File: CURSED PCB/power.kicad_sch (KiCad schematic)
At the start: 22 parts, among them J3 2 Wire Block for laser, J5 G125-MH104M4-04AD000P, U1 MIC94090YC6, U2 INA180, U4 SPX3819M5-L-3-3, U5 MCP1754S-3302xCB

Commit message: fix with ash
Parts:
- removed U5: MCP1754S-3302xCB, Package_TO_SOT_SMD:SOT-23, symbol Regulator_Linear:MCP1754S-3302xCB
- added U5: SPX3819M5-L-3-3, Package_TO_SOT_SMD:SOT-23-5, symbol Regulator_Linear:SPX3819M5-L-3-3
- C10: value 1uF -> 10nF
- C13: value 10uF -> 1uF
- F1: value 600mA -> 1A
- R6: value 55m -> 33m
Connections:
- net +3.3VA: now also U5.5 (OUT); no longer C10.1
- net +5V: now also U5.1 (IN), U5.3 (EN)
- net GND: now also U5.2 (GND)
- new net: C10.1, U5.4 (BP)
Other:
- note added: "100 V/V Gain or 40dB"
- note added: "R_shunt = (VOUT / GAIN)/ Current VOUT = 3.3 Gain = 100 Current = 1A R_shunt = 33 mohm"
- note removed: "100 Gain"
- moved on the sheet: C10
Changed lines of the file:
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@@
 	(generator_version "9.0")
 	(paper "A4")
-	(text "100 Gain\n"
+	(text "R_shunt = (VOUT / GAIN)/ Current\n\nVOUT = 3.3\nGain = 100\nCurrent = 1A\nR_shunt = 33 mohm"
 		(exclude_from_sim no)
-		(at 103.886 78.232 0)
+		(at 65.786 43.688 0)
+		(effects
+			(font
+				(size 1.27 1.27)
+			)
+		)
+	)
+	(text "100 V/V Gain or 40dB\n\n\n"
+		(exclude_from_sim no)
+		(at 114.046 83.058 0)
 		(effects
 			(font
@@
 	)
 	(junction
+		(at 176.53 88.9)
+		(diameter 0)
+		(color 0 0 0 0)
+	)
+	(junction
 		(at 214.63 54.61)
 		(diameter 0)
@@
 	)
 	(junction
-		(at 198.12 88.9)
-		(diameter 0)
-		(color 0 0 0 0)
-	)
-	(junction
 		(at 203.2 54.61)
 		(diameter 0)
@@
 	(wire
 		(pts
-			(xy 165.1 88.9) (xy 177.8 88.9)
+			(xy 165.1 88.9) (xy 176.53 88.9)
 		)
 		(stroke
@@
 	(wire
 		(pts
-			(xy 87.63 57.15) (xy 88.9 57.15)
+			(xy 177.8 91.44) (xy 176.53 91.44)
 		)
 		(stroke
@@
 	(wire
 		(pts
-			(xy 198.12 88.9) (xy 205.74 88.9)
+			(xy 87.63 57.15) (xy 88.9 57.15)
 		)
 		(stroke
@@
 	(wire
 		(pts
-			(xy 185.42 96.52) (xy 185.42 99.06)
+			(xy 193.04 88.9) (xy 205.74 88.9)
 		)
 		(stroke
@@
 	(wire
 		(pts
+			(xy 176.53 91.44) (xy 176.53 88.9)
+		)
+		(stroke
+			(width 0)
+			(type default)
+		)
+	)
+	(wire
+		(pts
 			(xy 95.25 82.55) (xy 95.25 87.63)
 		)
@@
 	(wire
 		(pts
-			(xy 198.12 96.52) (xy 198.12 99.06)
+			(xy 198.12 99.06) (xy 198.12 101.6)
 		)
 		(stroke
@@
 	(wire
 		(pts
-			(xy 45.72 86.36) (xy 54.61 86.36)
+			(xy 176.53 88.9) (xy 177.8 88.9)
 		)
 		(stroke
@@
 	(wire
 		(pts
-			(xy 153.67 88.9) (xy 165.1 88.9)
+			(xy 45.72 86.36) (xy 54.61 86.36)
 		)
 		(stroke
@@
 	(wire
 		(pts
-			(xy 193.04 88.9) (xy 198.12 88.9)
+			(xy 153.67 88.9) (xy 165.1 88.9)
 		)
 		(stroke
@@
 	(wire
 		(pts
+			(xy 185.42 99.06) (xy 185.42 105.41)
+		)
+		(stroke
+			(width 0)
+			(type default)
+		)
+	)
+	(wire
+		(pts
 			(xy 173.99 57.15) (xy 177.8 57.15)
 		)
@@
 	(wire
 		(pts
+			(xy 193.04 91.44) (xy 198.12 91.44)
+		)
+		(stroke
+			(width 0)
+			(type default)
+		)
+	)
+	(wire
+		(pts
 			(xy 39.37 106.68) (xy 29.21 106.68)
 		)
@@
 	(symbol
 		(lib_id "power:GND")
-		(at 185.42 99.06 0)
+		(at 185.42 105.41 0)
 		(unit 1)
 		(exclude_from_sim no)
@@
 		(fields_autoplaced yes)
 		(property "Reference" "#PWR029"
-			(at 185.42 105.41 0)
+			(at 185.42 111.76 0)
 			(effects
 				(font
@@
 		)
 		(property "Value" "GND"
-			(at 187.96 100.3299 0)
+			(at 187.96 106.6799 0)
 			(effects
 				(font
@@
 		)
 		(property "Footprint" ""
-			(at 185.42 99.06 0)
+			(at 185.42 105.41 0)
 			(effects
 				(font
@@
 		)
 		(property "Datasheet" ""
-			(at 185.42 99.06 0)
+			(at 185.42 105.41 0)
 			(effects
 				(font
@@
 		)
 		(property "Description" "Power symbol creates a global label with name \"GND\" , ground"
-			(at 185.42 99.06 0)
+			(at 185.42 105.41 0)
 			(effects
 				(font
@@
 			)
 		)
-		(property "Value" "600mA"
+		(property "Value" "1A"
 			(at 53.34 53.34 90)
 			(effects
@@
 	(symbol
 		(lib_id "power:GND")
-		(at 198.12 99.06 0)
+		(at 198.12 101.6 0)
 		(unit 1)
 		(exclude_from_sim no)
@@
 		(fields_autoplaced yes)
 		(property "Reference" "#PWR030"
-			(at 198.12 105.41 0)
+			(at 198.12 107.95 0)
 			(effects
 				(font
@@
 		)
 		(property "Value" "GND"
-			(at 200.66 100.3299 0)
+			(at 200.66 102.8699 0)
 			(effects
 				(font
@@
 		)
 		(property "Footprint" ""
-			(at 198.12 99.06 0)
+			(at 198.12 101.6 0)
 			(effects
 				(font
@@
 		)
 		(property "Datasheet" ""
-			(at 198.12 99.06 0)
+			(at 198.12 101.6 0)
 			(effects
 				(font
@@
 		)
 		(property "Description" "Power symbol creates a global label with name \"GND\" , ground"
-			(at 198.12 99.06 0)
+			(at 198.12 101.6 0)
 			(effects
 				(font
@@
 	)
 	(symbol
-		(lib_id "Regulator_Linear:MCP1754S-3302xCB")
-		(at 185.42 88.9 0)
-		(unit 1)
-		(exclude_from_sim no)
-		(in_bom yes)
-		(on_board yes)
-		(dnp no)
-		(fields_autoplaced yes)
-		(property "Reference" "U5"
-			(at 185.42 82.55 0)
-			(effects
-				(font
-					(size 1.27 1.27)
-				)
-			)
-		)
-		(property "Value" "MCP1754S-3302xCB"
-			(at 185.42 85.09 0)
-			(effects
-				(font
-					(size 1.27 1.27)
-				)
-			)
-		)
-		(property "Footprint" "Package_TO_SOT_SMD:SOT-23"
-			(at 185.42 83.185 0)
-			(effects
-				(font
-					(size 1.27 1.27)
-				)
-				(hide yes)
-			)
-		)
-		(property "Datasheet" "http://ww1.microchip.com/downloads/en/DeviceDoc/20002276C.pdf"
-			(at 185.42 88.9 0)
-			(effects
-				(font
-					(size 1.27 1.27)
-				)
-				(hide yes)
-			)
-		)
-		(property "Description" "Fixed 150mA Low Dropout Voltage Regulator, Positive, 3.3V output, SOT-23"
-			(at 185.42 88.9 0)
-			(effects
-				(font
-					(size 1.27 1.27)
-				)
-				(hide yes)
-			)
-		)
-		(pin "2"
-		)
-		(pin "3"
-		)
-		(pin "1"
-		)
-		(instances
-			(project ""
-				(path "/9fb1a86f-679c-4b88-9ed1-932f4f414580/78e664bb-f661-4ad0-951c-8ffe0c2483d0"
-					(reference "U5")
-					(unit 1)
-				)
-			)
-		)
-	)
-	(symbol
 		(lib_id "power:+3.3VA")
 		(at 88.9 45.72 0)
@@
 			)
 		)
-		(property "Value" "55m"
+		(property "Value" "33m"
 			(at 83.82 53.34 90)
 			(effects
@@
 			)
 		)
-		(property "Value" "10uF"
+		(property "Value" "1uF"
 			(at 223.52 93.9799 0)
 			(effects
@@
 	(symbol
 		(lib_id "PCM_Capacitor_US_AKL:C_0201")
-		(at 198.12 92.71 0)
+		(at 198.12 95.25 0)
 		(unit 1)
 		(exclude_from_sim no)
@@
 		(fields_autoplaced yes)
 		(property "Reference" "C10"
-			(at 201.93 91.4399 0)
+			(at 201.93 93.9799 0)
 			(effects
 				(font
@@
 			)
 		)
-		(property "Value" "1uF"
-			(at 201.93 93.9799 0)
+		(property "Value" "10nF"
+			(at 201.93 96.5199 0)
 			(effects
 				(font
@@
 		)
 		(property "Footprint" "Capacitor_SMD:C_0805_2012Metric_Pad1.18x1.45mm_HandSolder"
-			(at 199.0852 96.52 0)
+			(at 199.0852 99.06 0)
 			(effects
 				(font
@@
 		)
 		(property "Datasheet" "~"
-			(at 198.12 92.71 0)
+			(at 198.12 95.25 0)
 			(effects
 				(font
@@
 		)
 		(property "Description" "SMD 0201 MLCC capacitor, Alternate KiCad Library"
-			(at 198.12 92.71 0)
+			(at 198.12 95.25 0)
 			(effects
 				(font
@@
 					(unit 1)
 				)
+			)
+		)
+	)
+	(symbol
+		(lib_id "Regulator_Linear:SPX3819M5-L-3-3")
+		(at 185.42 91.44 0)
+		(unit 1)
+		(exclude_from_sim no)
+		(in_bom yes)
+		(on_board yes)
+		(dnp no)
+		(fields_autoplaced yes)
+		(property "Reference" "U5"
+			(at 185.42 82.55 0)
+			(effects
+				(font
+					(size 1.27 1.27)
+				)
+			)
+		)
+		(property "Value" "SPX3819M5-L-3-3"
+			(at 185.42 85.09 0)
+			(effects
+				(font
+					(size 1.27 1.27)
+				)
+			)
+		)
+		(property "Footprint" "Package_TO_SOT_SMD:SOT-23-5"
+			(at 185.42 83.185 0)
+			(effects
+				(font
+					(size 1.27 1.27)
+				)
+				(hide yes)
+			)
+		)
+		(property "Datasheet" "https://www.exar.com/content/document.ashx?id=22106&languageid=1033&type=Datasheet&partnumber=SPX3819&filename=SPX3819.pdf&part=SPX3819"
+			(at 185.42 91.44 0)
+			(effects
+				(font
+					(size 1.27 1.27)
+				)
+				(hide yes)
+			)
+		)
+		(property "Description" "500mA Low drop-out regulator, Fixed Output 3.3V, SOT-23-5"
+			(at 185.42 91.44 0)
+			(effects
+				(font
+					(size 1.27 1.27)
+				)
+				(hide yes)
+			)
+		)
+		(pin "3"
+		)
+		(pin "2"
+		)
+		(pin "1"
+		)
+		(pin "5"
+		)
+		(pin "4"
+		)
+		(instances
+			(project "sensor_1"
+				(path "/9fb1a86f-679c-4b88-9ed1-932f4f414580/78e664bb-f661-4ad0-951c-8ffe0c2483d0"
+					(reference "U5")
+					(unit 1)
+				)

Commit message: push
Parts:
- U2: value INA180 -> INA180-A3
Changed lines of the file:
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@@
 		(fields_autoplaced yes)
 		(property "Reference" "U2"
-			(at 107.95 68.5098 0)
-			(effects
-				(font
-					(size 1.27 1.27)
-				)
-			)
-		)
-		(property "Value" "INA180"
-			(at 107.95 71.0498 0)
+			(at 109.22 68.5098 0)
+			(effects
+				(font
+					(size 1.27 1.27)
+				)
+			)
+		)
+		(property "Value" "INA180-A3"
+			(at 109.22 71.0498 0)
 			(effects
 				(font
@@
 			)
 		)
-		(property "Datasheet" "https://www.exar.com/content/document.ashx?id=22106&languageid=1033&type=Datasheet&partnumber=SPX3819&filename=SPX3819.pdf&part=SPX3819"
+		(property "Datasheet" "https://mm.digikey.com/Volume0/opasdata/d220001/medias/docus/6642/1016_SPX3819.pdf"
 			(at 185.42 57.15 0)
 			(effects
@@
 			)
 		)
-		(property "Datasheet" "https://www.exar.com/content/document.ashx?id=22106&languageid=1033&type=Datasheet&partnumber=SPX3819&filename=SPX3819.pdf&part=SPX3819"
+		(property "Datasheet" "https://mm.digikey.com/Volume0/opasdata/d220001/medias/docus/6642/1016_SPX3819.pdf"
 			(at 185.42 91.44 0)
 			(effects

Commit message: updated schematic
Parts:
- removed J3: 2 Wire Block for laser, 691137710002:691137710002, symbol 691137710002:691137710002
- removed JP4: SolderJumper_2_Open, Jumper:SolderJumper-2_P1.3mm_Open_Pad1.0x1.5mm, symbol Jumper:SolderJumper_2_Open
- removed U1: MIC94090YC6, Package_TO_SOT_SMD:SOT-363_SC-70-6, symbol Power_Management:MIC94090YC6
- added C32: 0.1uF, Capacitor_SMD:C_0805_2012Metric_Pad1.18x1.45mm_HandSolder, symbol PCM_Capacitor_US_AKL:C_0201
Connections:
- net +3.3VD: now also C32.1
- net GND: now also C32.2

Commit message: updated schematic
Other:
- note removed: "Laser: https://www.iadiy.com/infrared-laser-module-LM9IR830H200D&path=168_173"
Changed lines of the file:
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@@
-		)
-	)
-	(text "Laser: https://www.iadiy.com/infrared-laser-module-LM9IR830H200D&path=168_173"
-		(exclude_from_sim no)
-		(at 58.928 132.842 0)
-		(effects
-			(font
-				(size 1.27 1.27)
-			)
 		)
 	)
@@
 		(on_board yes)
 		(dnp no)
-		(fields_autoplaced yes)
 		(property "Reference" "C32"
-			(at 101.6 57.15 90)
+			(at 112.268 60.198 90)
 			(effects
 				(font
@@
 		)
 		(property "Value" "0.1uF"
-			(at 101.6 59.69 90)
-			(effects
-				(font
+			(at 113.03 62.23 90)
+			(effects
+				(font

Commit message: schematic changes
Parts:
- renumbered TP2 to 3V3DTP1, TP3 to 3V3TP1, TP6 to 5VTP1
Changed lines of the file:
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@@
 		(on_board yes)
 		(dnp no)
-		(property "Reference" "TP2"
+		(property "Reference" "3V3DTP1"
 			(at 205.74 50.292 0)
 			(effects
@@
 			(project "sensor_1"
 				(path "/9fb1a86f-679c-4b88-9ed1-932f4f414580/78e664bb-f661-4ad0-951c-8ffe0c2483d0"
-					(reference "TP2")
+					(reference "3V3DTP1")
 					(unit 1)
 				)
@@
 		(on_board yes)
 		(dnp no)
-		(property "Reference" "TP3"
+		(property "Reference" "3V3TP1"
 			(at 208.026 84.836 0)
 			(effects
@@
 			(project "sensor_1"
 				(path "/9fb1a86f-679c-4b88-9ed1-932f4f414580/78e664bb-f661-4ad0-951c-8ffe0c2483d0"
-					(reference "TP3")
+					(reference "3V3TP1")
 					(unit 1)
 				)
@@
 		(on_board yes)
 		(dnp no)
-		(property "Reference" "TP6"
+		(property "Reference" "5VTP1"
 			(at 101.6 52.832 0)
 			(effects
@@
 			(project "sensor_1"
 				(path "/9fb1a86f-679c-4b88-9ed1-932f4f414580/78e664bb-f661-4ad0-951c-8ffe0c2483d0"
-					(reference "TP6")
-					(unit 1)
-				)
+					(reference "5VTP1")
+					(unit 1)
+				)

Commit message: footprint folde rupdate
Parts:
- F1: footprint Fuse:Fuse_Bourns_MF-RG300 -> Fuse:Fuse_1206_3216Metric_Pad1.42x1.75mm_HandSolder
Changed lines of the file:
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@@
 			)
 		)
-		(property "Footprint" "Fuse:Fuse_Bourns_MF-RG300"
+		(property "Footprint" "Fuse:Fuse_1206_3216Metric_Pad1.42x1.75mm_HandSolder"
 			(at 58.42 55.88 0)
 			(effects

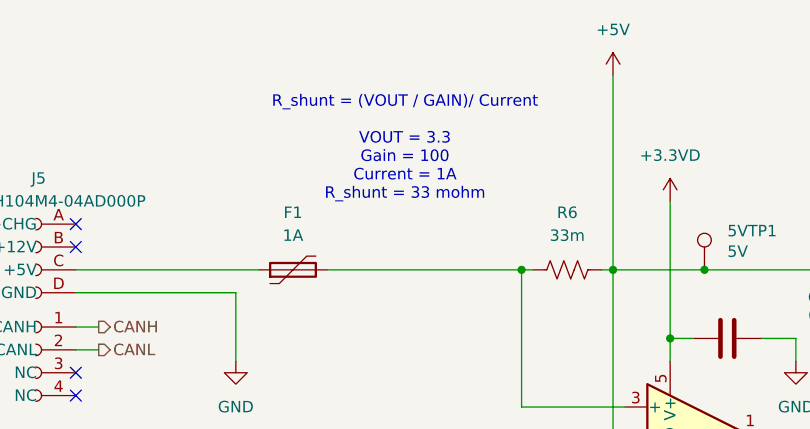
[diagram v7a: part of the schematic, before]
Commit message: Updated PDF and make schematic look more pretty
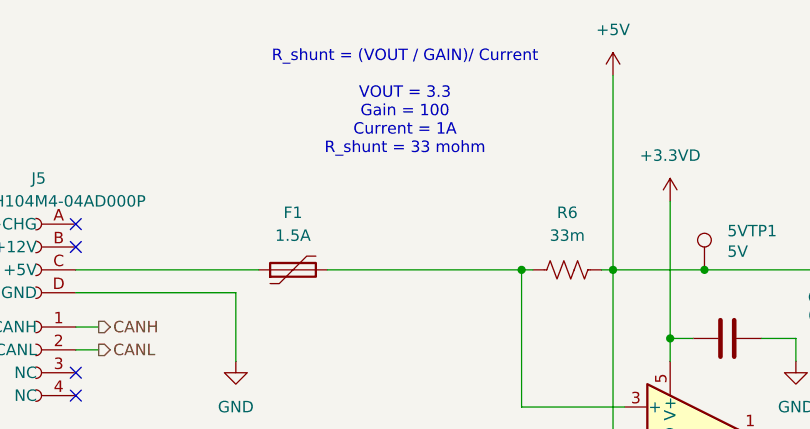
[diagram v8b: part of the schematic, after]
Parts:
- F1: value 1A -> 1.5A
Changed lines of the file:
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@@
 	(text "R_shunt = (VOUT / GAIN)/ Current\n\nVOUT = 3.3\nGain = 100\nCurrent = 1A\nR_shunt = 33 mohm"
 		(exclude_from_sim no)
-		(at 65.786 43.688 0)
+		(at 65.786 38.608 0)
 		(effects
 			(font
@@
 			)
 		)
-		(property "Value" "1A"
+		(property "Value" "1.5A"
 			(at 53.34 53.34 90)
 			(effects
